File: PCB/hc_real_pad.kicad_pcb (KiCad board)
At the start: 2 copper layers, 149.9 x 81.3 mm, 55 parts, among them J1 OLED_DISPLAY, SW1 SW_Push_45deg, SW10 SW_Push_45deg, SW11 SW_Push_45deg, SW12 SW_Push_45deg, SW13 SW_Push_45deg, SW14 SW_Push_45deg, SW15 SW_Push_45deg, SW16 SW_Push_45deg, SW17 RotaryEncoder_Switch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

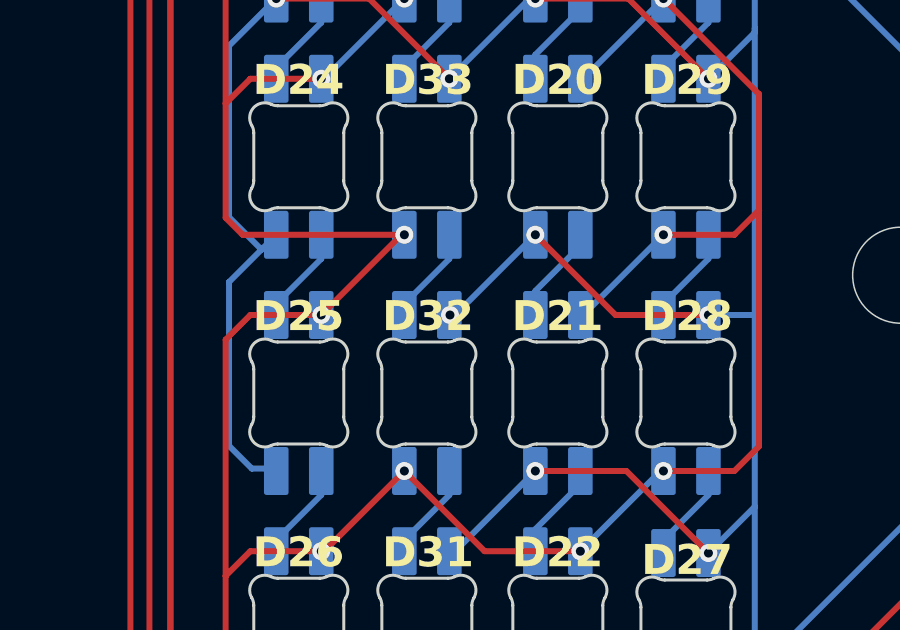
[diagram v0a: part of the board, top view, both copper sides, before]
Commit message: added assembly and updated readme
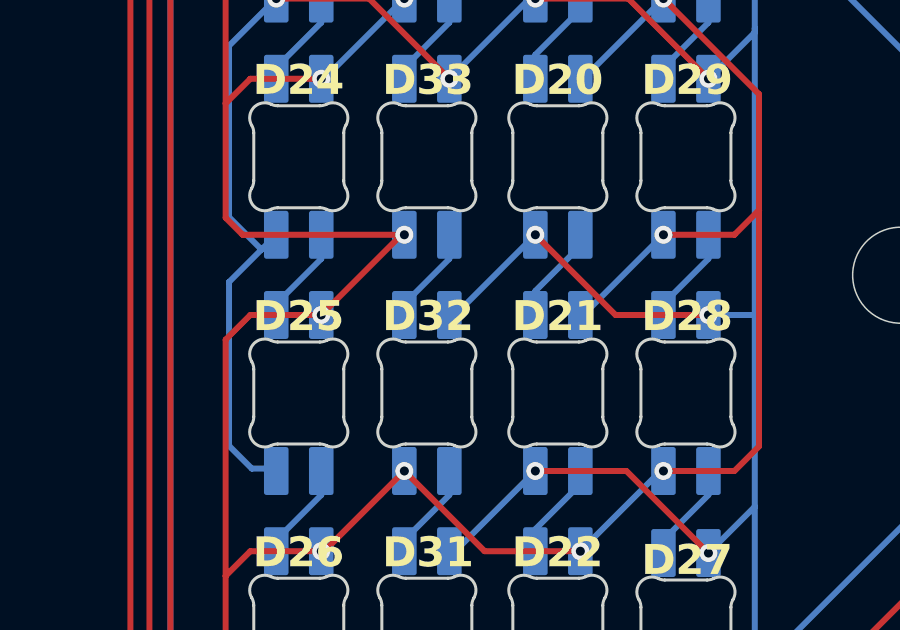
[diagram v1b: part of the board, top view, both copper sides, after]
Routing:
- net VCC: vias 11 -> 10
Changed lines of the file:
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@@
-	)
-	(via
-		(at 70.978316 139.326002)
-		(size 0.6)
-		(drill 0.3)
-		(layers "F.Cu" "B.Cu")
-		(net 26)
 	)
 	(via

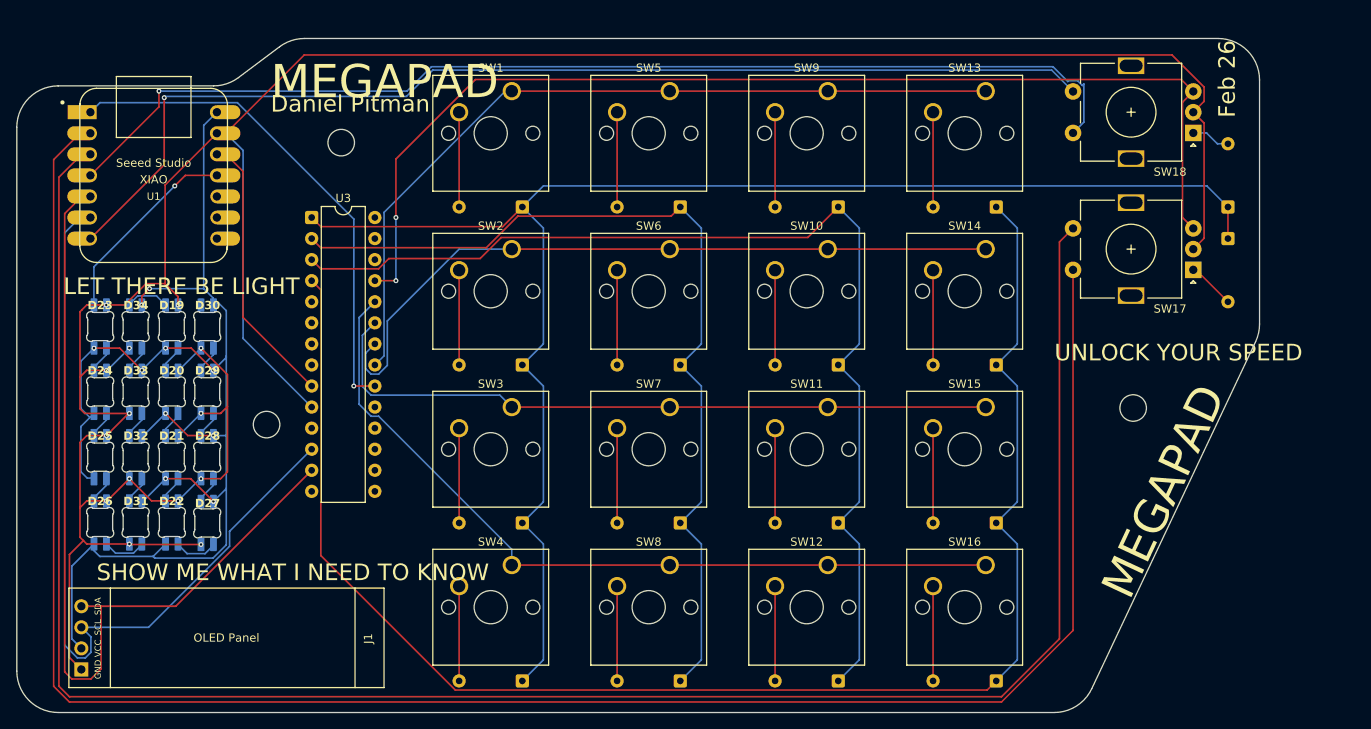
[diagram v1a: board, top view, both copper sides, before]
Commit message: added ground planes
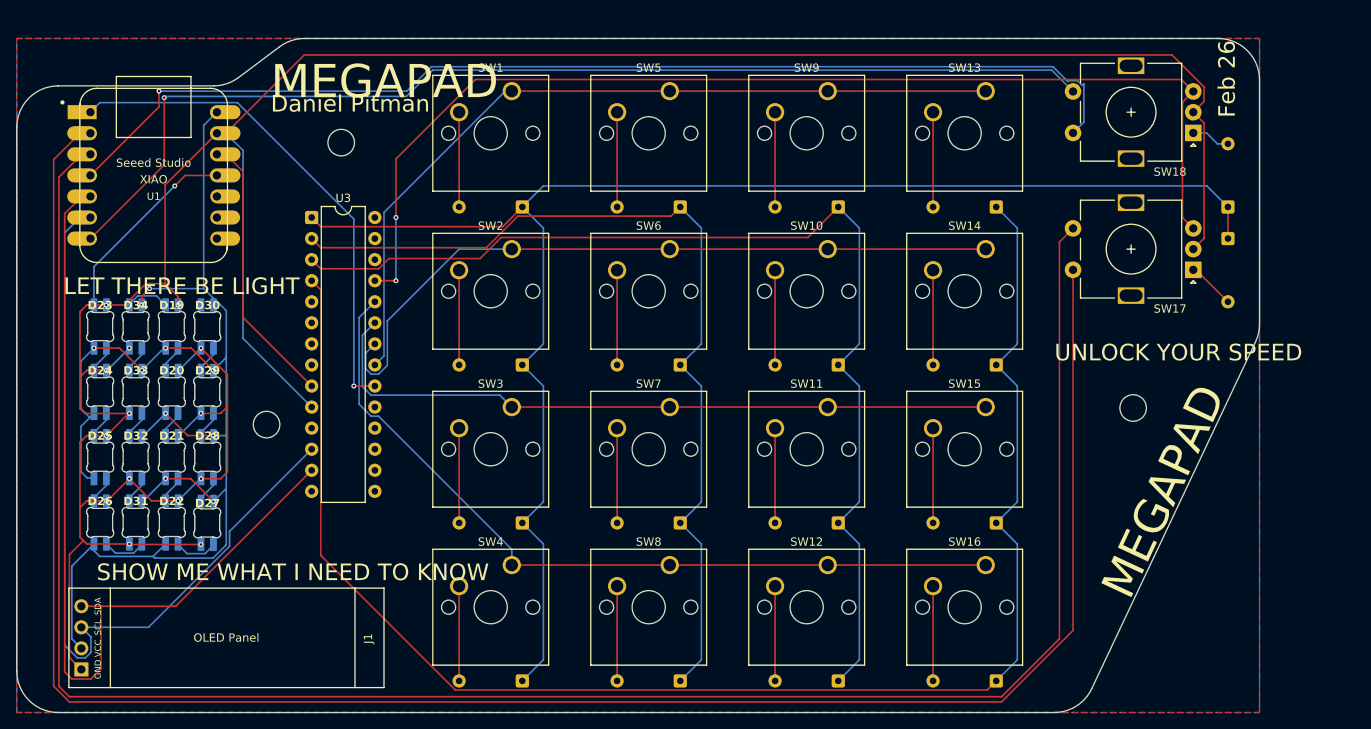
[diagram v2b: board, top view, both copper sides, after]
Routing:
- added copper zone on B.Cu, net GND
- added copper zone on F.Cu, net GND
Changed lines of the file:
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@@
 		(net 57)
+	)
+	(zone
+		(net 24)
+		(net_name "GND")
+		(layer "F.Cu")
+		(hatch edge 0.5)
+		(connect_pads
+			(clearance 0.5)
+		)
+		(min_thickness 0.25)
+		(filled_areas_thickness no)
+		(fill yes
+			(thermal_gap 0.5)
+			(thermal_bridge_width 0.5)
+		)
+		(polygon
+			(pts
+				(xy 55.88 172.72) (xy 205.74 172.72) (xy 205.74 91.44) (xy 55.88 91.44)
+			)
+		)
+	)
+	(zone
+		(net 24)
+		(net_name "GND")
+		(layer "B.Cu")
+		(hatch edge 0.5)
+		(priority 1)
+		(connect_pads
+			(clearance 0.5)
+		)
+		(min_thickness 0.25)
+		(filled_areas_thickness no)
+		(fill yes
+			(thermal_gap 0.5)
+			(thermal_bridge_width 0.5)
+		)
+		(polygon
+			(pts
+				(xy 55.88 91.44) (xy 205.74 91.44) (xy 205.74 172.72) (xy 55.88 172.72)
+			)
+		)
 	)
 	(embedded_fonts no)
